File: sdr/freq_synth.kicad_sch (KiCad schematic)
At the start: 9 parts, among them U1 MS5351M, Y1 25MHz

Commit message: Update lots of things. Now have basic CPU as well as some crude mixers
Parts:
- renumbered U1 to U2
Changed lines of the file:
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@@
   (symbol (lib_id "power:GND") (at 149.86 111.76 0) (unit 1)
     (in_bom yes) (on_board yes) (fields_autoplaced)
-    (property "Reference" "#PWR09" (id 0) (at 149.86 118.11 0)
+    (property "Reference" "#PWR012" (id 0) (at 149.86 118.11 0)
       (effects (font (size 1.27 1.27)) hide)
     )
@@
   (symbol (lib_id "power:+3.3V") (at 147.32 72.39 0) (unit 1)
     (in_bom yes) (on_board yes) (fields_autoplaced)
-    (property "Reference" "#PWR08" (id 0) (at 147.32 76.2 0)
+    (property "Reference" "#PWR011" (id 0) (at 147.32 76.2 0)
       (effects (font (size 1.27 1.27)) hide)
     )
@@
   (symbol (lib_id "power:GND") (at 128.27 109.22 0) (unit 1)
     (in_bom yes) (on_board yes) (fields_autoplaced)
-    (property "Reference" "#PWR06" (id 0) (at 128.27 115.57 0)
+    (property "Reference" "#PWR09" (id 0) (at 128.27 115.57 0)
       (effects (font (size 1.27 1.27)) hide)
     )
@@
   (symbol (lib_id "power:GND") (at 157.48 80.01 0) (unit 1)
     (in_bom yes) (on_board yes) (fields_autoplaced)
-    (property "Reference" "#PWR010" (id 0) (at 157.48 86.36 0)
+    (property "Reference" "#PWR013" (id 0) (at 157.48 86.36 0)
       (effects (font (size 1.27 1.27)) hide)
     )
@@
   (symbol (lib_id "zl4aa:MS5351M") (at 149.86 95.25 0) (unit 1)
     (in_bom yes) (on_board yes) (fields_autoplaced)
-    (property "Reference" "U1" (id 0) (at 151.8794 108.585 0)
+    (property "Reference" "U2" (id 0) (at 151.8794 108.585 0)
       (effects (font (size 1.27 1.27)) (justify left))
     )
@@
   (symbol (lib_id "power:GND") (at 140.97 80.01 0) (unit 1)
     (in_bom yes) (on_board yes) (fields_autoplaced)
-    (property "Reference" "#PWR07" (id 0) (at 140.97 86.36 0)
-      (effects (font (size 1.27 1.27)) hide)
-    )
+    (property "Reference" "#PWR010" (id 0) (at 140.97 86.36 0)
+      (effects (font (size 1.27 1.27)) hide)
+    )

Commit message: Added ST-link 6-pin 0.1 programming header
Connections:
- net SCL: no longer R4.2, U2.5 (SDA)
- new net SDA: R4.2, U2.5 (SDA)
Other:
- moved on the sheet: R4, R5
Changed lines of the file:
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@@
   (junction (at 119.38 100.33) (diameter 0) (color 0 0 0 0)
   )
-  (junction (at 111.76 100.33) (diameter 0) (color 0 0 0 0)
-  )
   (junction (at 152.4 72.39) (diameter 0) (color 0 0 0 0)
   )
@@
     (stroke (width 0) (type default) (color 0 0 0 0))
   )
+  (wire (pts (xy 119.38 88.9) (xy 119.38 100.33))
+    (stroke (width 0) (type default) (color 0 0 0 0))
+  )
   (wire (pts (xy 119.38 100.33) (xy 137.16 100.33))
     (stroke (width 0) (type default) (color 0 0 0 0))
@@
     (stroke (width 0) (type default) (color 0 0 0 0))
   )
-  (wire (pts (xy 119.38 72.39) (xy 119.38 92.71))
+  (wire (pts (xy 119.38 72.39) (xy 119.38 81.28))
     (stroke (width 0) (type default) (color 0 0 0 0))
   )
@@
     (stroke (width 0) (type default) (color 0 0 0 0))
   )
-  (wire (pts (xy 111.76 102.87) (xy 111.76 100.33))
-    (stroke (width 0) (type default) (color 0 0 0 0))
-  )
-  (wire (pts (xy 111.76 100.33) (xy 119.38 100.33))
-    (stroke (width 0) (type default) (color 0 0 0 0))
-  )
-  (wire (pts (xy 111.76 72.39) (xy 111.76 92.71))
+  (wire (pts (xy 111.76 91.44) (xy 111.76 102.87))
+    (stroke (width 0) (type default) (color 0 0 0 0))
+  )
+  (wire (pts (xy 97.79 100.33) (xy 119.38 100.33))
+    (stroke (width 0) (type default) (color 0 0 0 0))
+  )
+  (wire (pts (xy 111.76 72.39) (xy 111.76 83.82))
     (stroke (width 0) (type default) (color 0 0 0 0))
   )
@@
   )
   (wire (pts (xy 147.32 72.39) (xy 140.97 72.39))
-    (stroke (width 0) (type default) (color 0 0 0 0))
-  )
-  (wire (pts (xy 97.79 100.33) (xy 111.76 100.33))
     (stroke (width 0) (type default) (color 0 0 0 0))
   )
@@
     (pin "1")
   )
-  (symbol (lib_id "Device:R") (at 111.76 96.52 0) (unit 1)
-    (in_bom yes) (on_board yes) (fields_autoplaced)
-    (property "Reference" "R4" (id 0) (at 114.3 95.2499 0)
-      (effects (font (size 1.27 1.27)) (justify left))
-    )
-    (property "Value" "10k" (id 1) (at 114.3 97.7899 0)
-      (effects (font (size 1.27 1.27)) (justify left))
-    )
-    (property "Footprint" "Resistor_SMD:R_0402_1005Metric" (id 2) (at 109.982 96.52 90)
-      (effects (font (size 1.27 1.27)) hide)
-    )
-    (property "Datasheet" "~" (id 3) (at 111.76 96.52 0)
+  (symbol (lib_id "Device:R") (at 111.76 87.63 0) (unit 1)
+    (in_bom yes) (on_board yes) (fields_autoplaced)
+    (property "Reference" "R4" (id 0) (at 114.3 86.3599 0)
+      (effects (font (size 1.27 1.27)) (justify left))
+    )
+    (property "Value" "10k" (id 1) (at 114.3 88.8999 0)
+      (effects (font (size 1.27 1.27)) (justify left))
+    )
+    (property "Footprint" "Resistor_SMD:R_0402_1005Metric" (id 2) (at 109.982 87.63 90)
+      (effects (font (size 1.27 1.27)) hide)
+    )
+    (property "Datasheet" "~" (id 3) (at 111.76 87.63 0)
       (effects (font (size 1.27 1.27)) hide)
     )
@@
     (pin "9")
   )
-  (symbol (lib_id "Device:R") (at 119.38 96.52 0) (unit 1)
-    (in_bom yes) (on_board yes) (fields_autoplaced)
-    (property "Reference" "R5" (id 0) (at 121.92 95.2499 0)
-      (effects (font (size 1.27 1.27)) (justify left))
-    )
-    (property "Value" "10k" (id 1) (at 121.92 97.7899 0)
-      (effects (font (size 1.27 1.27)) (justify left))
-    )
-    (property "Footprint" "Resistor_SMD:R_0402_1005Metric" (id 2) (at 117.602 96.52 90)
-      (effects (font (size 1.27 1.27)) hide)
-    )
-    (property "Datasheet" "~" (id 3) (at 119.38 96.52 0)
-      (effects (font (size 1.27 1.27)) hide)
-    )
+  (symbol (lib_id "Device:R") (at 119.38 85.09 0) (unit 1)
+    (in_bom yes) (on_board yes) (fields_autoplaced)
+    (property "Reference" "R5" (id 0) (at 121.92 83.8199 0)
+      (effects (font (size 1.27 1.27)) (justify left))
+    )
+    (property "Value" "10k" (id 1) (at 121.92 86.3599 0)
+      (effects (font (size 1.27 1.27)) (justify left))
+    )
+    (property "Footprint" "Resistor_SMD:R_0402_1005Metric" (id 2) (at 117.602 85.09 90)
+      (effects (font (size 1.27 1.27)) hide)
+    )
+    (property "Datasheet" "~" (id 3) (at 119.38 85.09 0)
+      (effects (font (size 1.27 1.27)) hide)
+    )

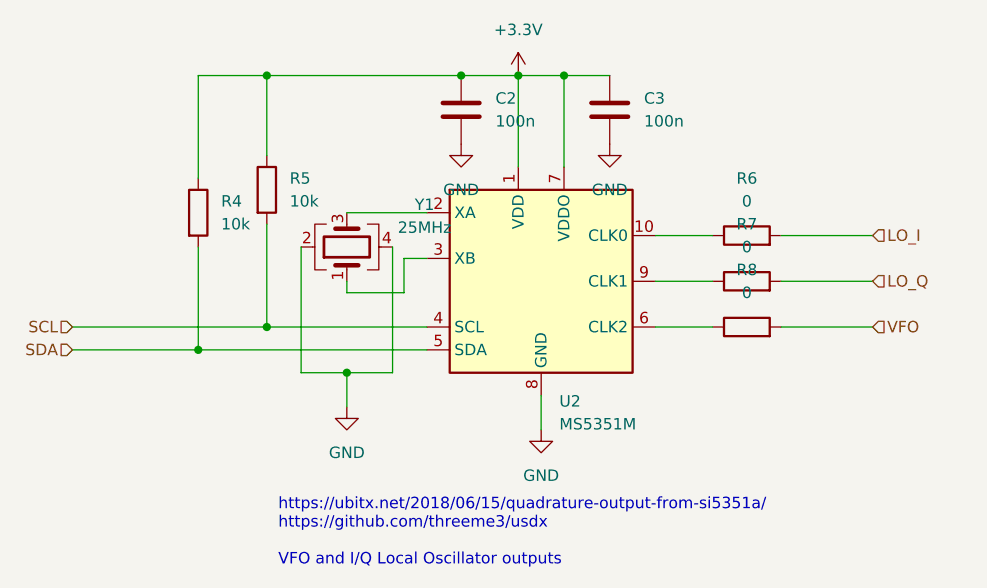
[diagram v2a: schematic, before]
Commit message: Tighten up design layout.
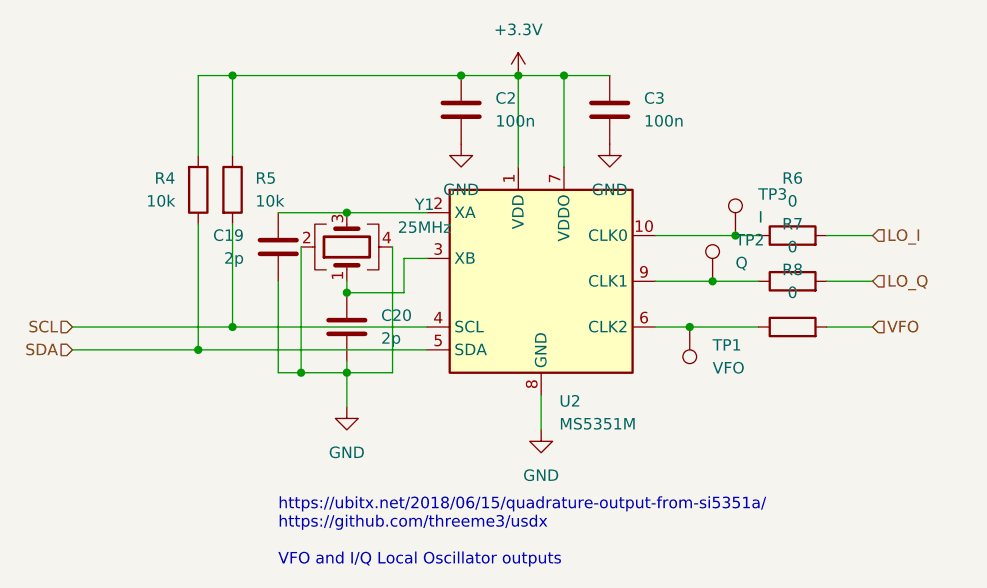
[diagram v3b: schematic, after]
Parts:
- added C19, C20: 2p, Capacitor_SMD:C_0402_1005Metric, symbol Device:C
- added TP1: VFO, TestPoint:TestPoint_Pad_D1.0mm, symbol Connector:TestPoint
- added TP2: Q, TestPoint:TestPoint_Pad_D1.0mm, symbol Connector:TestPoint
- added TP3: I, TestPoint:TestPoint_Pad_D1.0mm, symbol Connector:TestPoint
- C2, C3: footprint Capacitor_SMD:C_0603_1608Metric -> Capacitor_SMD:C_0402_1005Metric
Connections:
- net +3.3V: now also R4.2; no longer R4.1
- net GND: now also C19.1, C20.2
- net SDA: now also R4.1; no longer R4.2
- net at R6.1, U2.10 (CLK0): now also TP3.1
- net at U2.3 (XB), Y1.1: now also C20.1
- net at U2.2 (XA), Y1.3: now also C19.2
- net at R8.1, U2.6 (CLK2): now also TP1.1
- net at R7.1, U2.9 (CLK1): now also TP2.1
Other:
- moved on the sheet: R4, R5, R6, R7, R8
